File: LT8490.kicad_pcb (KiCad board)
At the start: 6 copper layers, 37.2 x 46 mm, 139 parts, among them J1 Conn_01x01, J10 Conn_01x01, J11 Conn_01x01, J12 Conn_01x01, J13 Conn_01x01, J14 Conn_01x01, J15 Conn_01x01, J16 Conn_01x01, J17 Conn_01x01, J18 Conn_01x01, J19 Conn_01x01, J2 Conn_01x01, J20 Conn_01x01, J21 Conn_01x01, J22 Conn_01x01, J23 Conn_01x01, J24 Conn_01x01, J25 Conn_01x01, J3 Conn_01x01, J4 Conn_01x01, J5 Conn_01x01, J6 Conn_01x01, J7 Conn_01x01, J8 Conn_01x01, J9 Conn_01x01, Q1 Si7106DN, Q2 Si7106DN, Q3 Si7106DN, Q4 Si7106DN, Q5 BSS84, Q6 MBT2222ADW1T1, U4 LT8490EUKJPBF

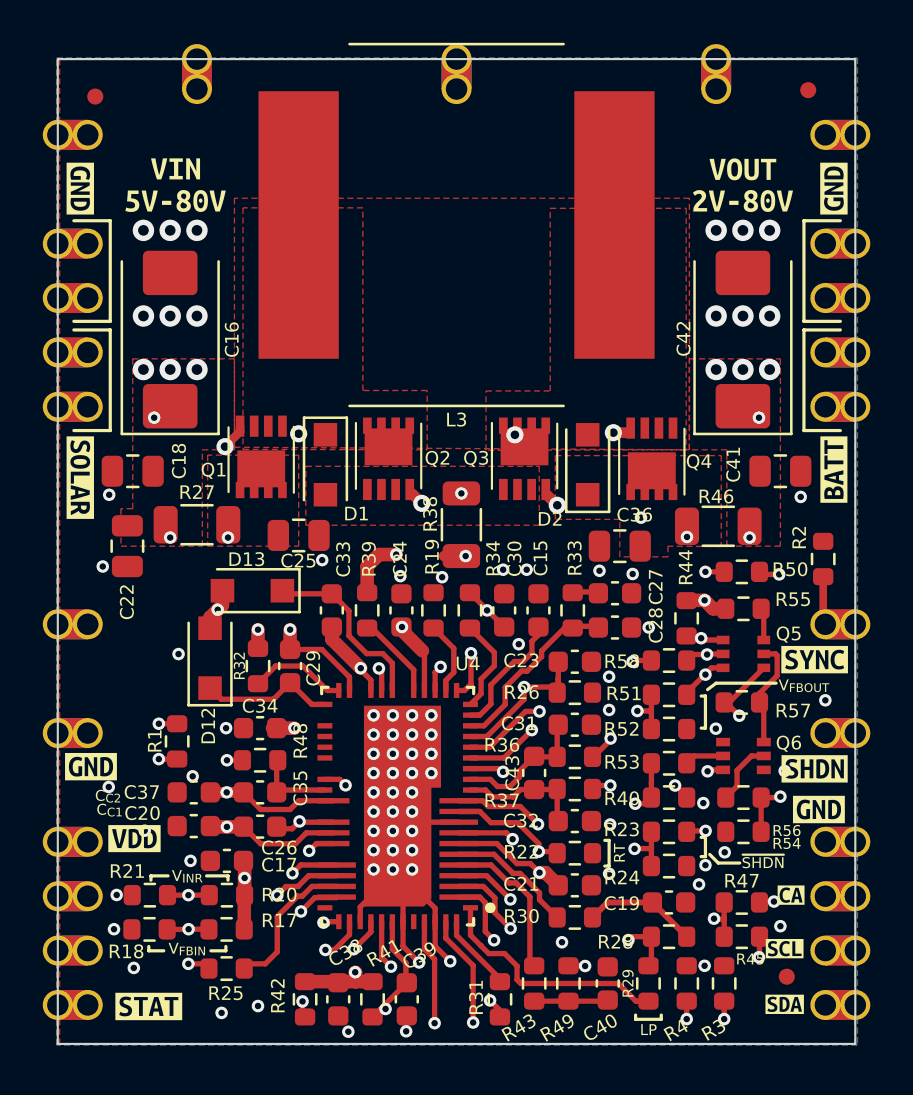
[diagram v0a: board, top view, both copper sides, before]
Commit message: shift big caps 2mm
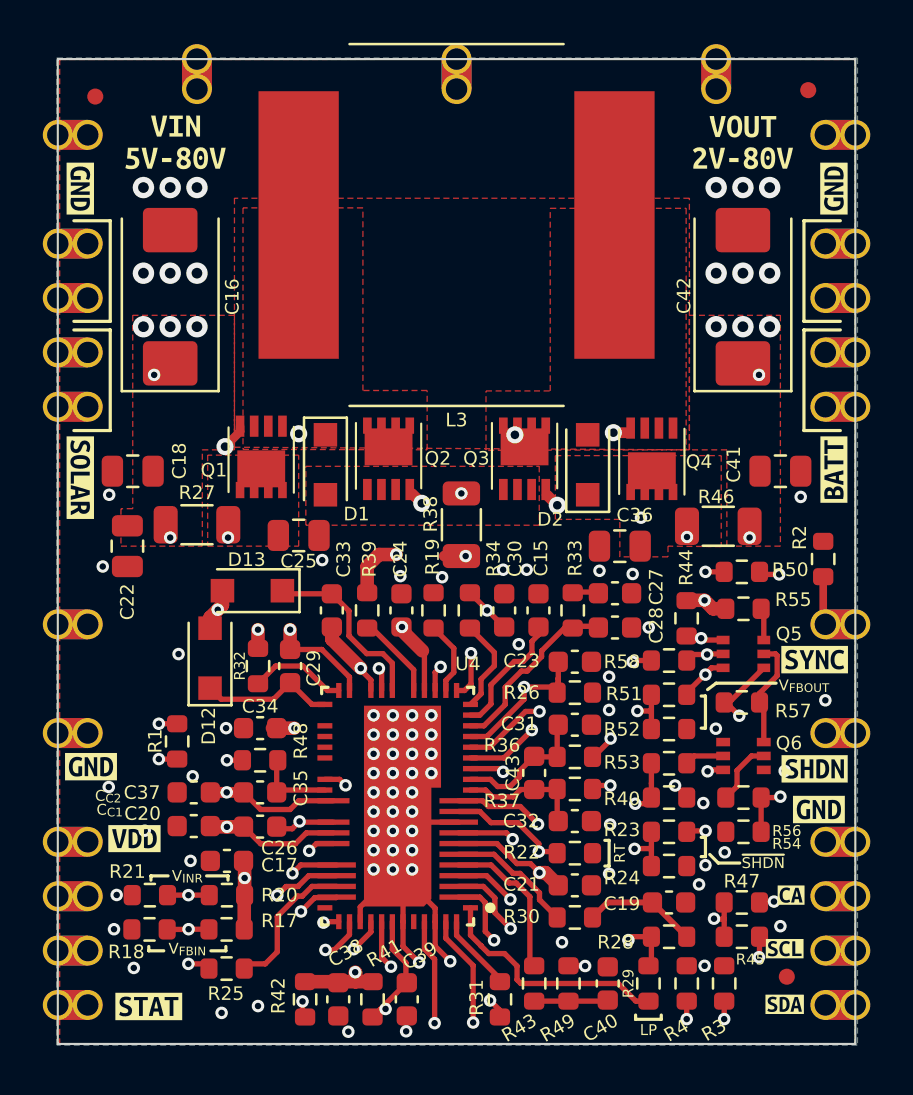
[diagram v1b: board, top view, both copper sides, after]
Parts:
- moved C16 2.00 mm to (134.5, 86.8)
- moved C42 2.00 mm to (161.2, 86.8)
- moved NT6 2.00 mm to (134.1, 90.1)
- moved NT7 2.00 mm to (161.6, 90.1)
- moved kibuzzard-623CCAD0 2.00 mm to (134.8, 78.9)
- moved kibuzzard-623CCAFA 2.00 mm to (134.8, 80.4)
- moved kibuzzard-623CCB0B 2.00 mm to (161.2, 80.4)
- moved kibuzzard-623CCB15 2.00 mm to (161.2, 78.9)

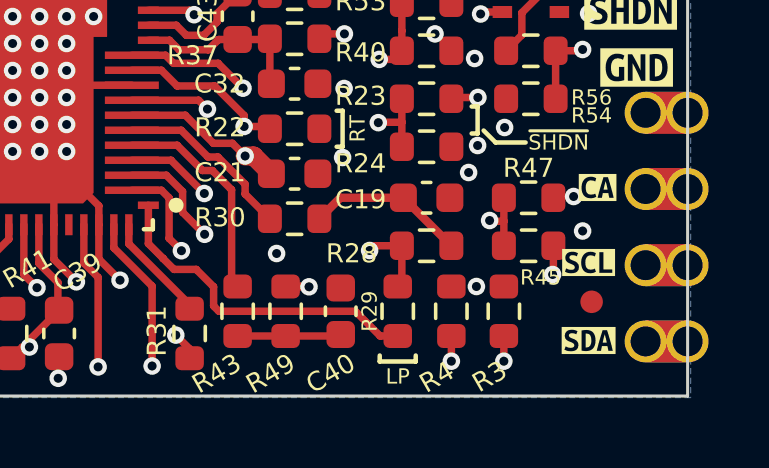
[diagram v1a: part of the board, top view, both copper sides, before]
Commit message: plane cleanup
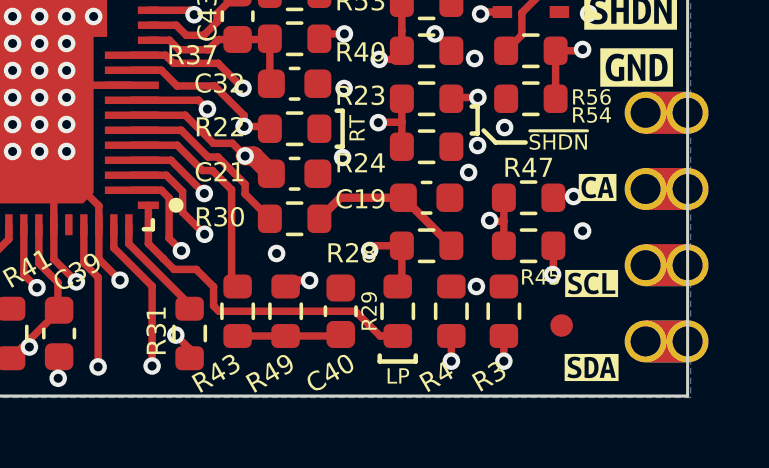
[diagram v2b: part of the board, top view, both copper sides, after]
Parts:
- moved REF** 1.27 mm to (162.3, 119.4)
- moved kibuzzard-623E06FB 0.91 mm to (163.3, 120.8)
- moved kibuzzard-623E06ED 0.71 mm to (163.3, 118.0)

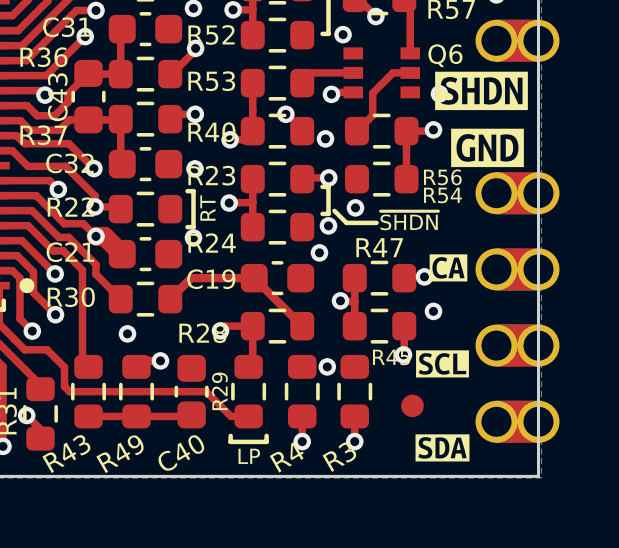
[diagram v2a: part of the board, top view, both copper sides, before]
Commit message: added i2c address resistors to CA
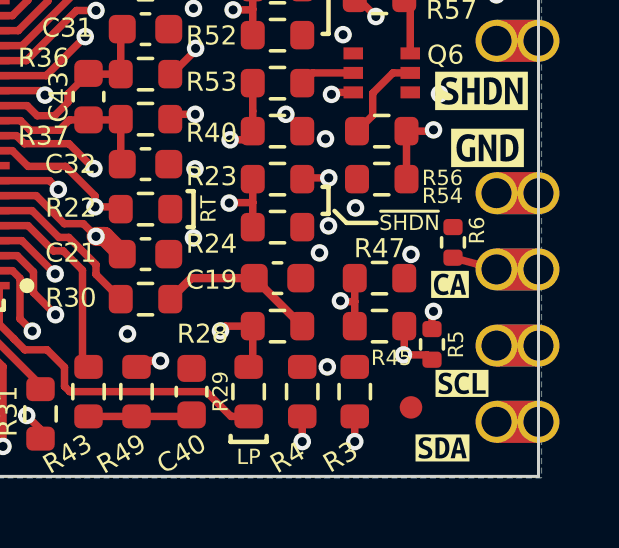
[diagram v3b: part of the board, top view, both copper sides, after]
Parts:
- added R5: 0, Resistor_SMD:R_0402_1005Metric, F.Cu at (162.9, 117.3)
- added R6: 0, Resistor_SMD:R_0402_1005Metric, F.Cu at (163.7, 114.0)
- moved kibuzzard-623E06ED 0.92 mm to (163.9, 118.7)
- moved kibuzzard-623E06E1 0.55 mm to (163.6, 115.3)
- moved REF** 0.07 mm to (162.2, 119.5)
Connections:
- net Net-(C39-Pad2) renamed /AVDD
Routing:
- net Net-(C25-Pad1): track 0.00 -> 12.6 mm, vias 0 -> 1
- net /CSNIN: track 12.6 -> 0.00 mm, vias 2 -> 1
- net REG_{FAULT}: track 21.5 -> 23.6 mm
- net /FBOUT: track 19.5 -> 21.5 mm
- net /FBIN: track 59.8 -> 61.8 mm
- net /AVDD: track 25.1 -> 26.1 mm
